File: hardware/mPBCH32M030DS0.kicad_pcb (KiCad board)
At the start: 2 copper layers, 20.3 x 53.3 mm, 90 parts, among them J1 EDGE_L, J2 EDGE_R, J8 USB-C, SW1 RESET, SW2 USER/BOOT, U1 CH32M030C8U7, U3 USBLC6-2SC6, Y1 8MHz CL=20pF

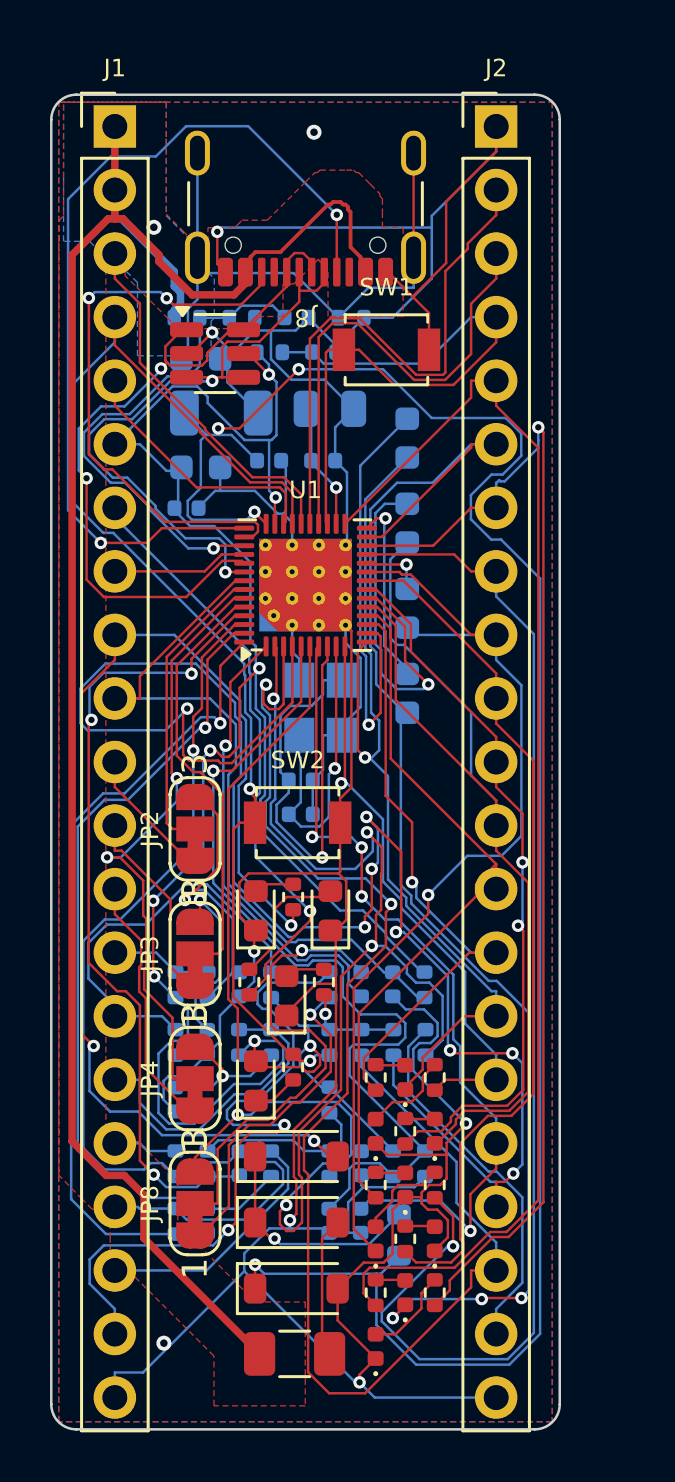
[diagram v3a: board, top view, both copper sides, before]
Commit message: 9マス版に一本化 (8マス版を削除)
- 8 マス版 (20.32mm) は JLCPCB の 2 層標準 0.127mm で配線しきれないため削除
- 9 マス版 (22.86mm, 端子列 0.7in) を hardware/ 直下・hardware/daughter/・hardware/fab/・docs/pcb/ へ移動
- ベタなし版は hardware/nopour/ (図は docs/pcb/nopour/)
- gen_pcb.py から MPB_W9 の切り替えを外し 9 マス固定に。既定ルールは 0.127mm / ビア 0.6/0.3
  (再生成した配置が確定済みの 4 基板と一致することを確認)
- 回路図の注記 (外形・列間) を 22.86mm / 17.78mm に更新し PDF を再出力
- README / stacking.md / design.md を 9 マス版のみの記述に更新

Co-Authored-By: Claude Opus 5.5 <noreply@anthropic.com>
Claude-Session: https://claude.ai/code/session_01LENFjjhDfYjJZV1NWhB9uV
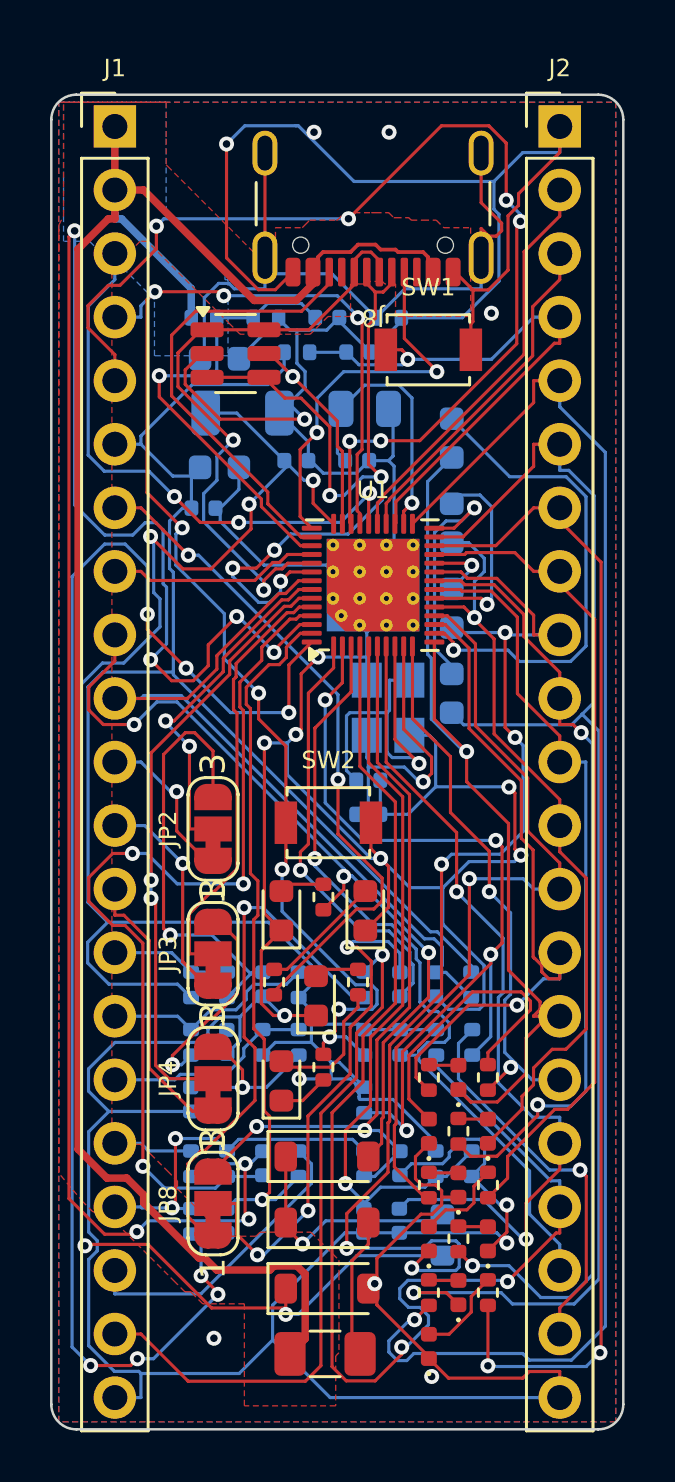
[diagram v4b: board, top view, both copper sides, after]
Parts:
- moved J8 2.70 mm to (12.9, 3.41)
- moved U1 2.70 mm to (12.9, 19.6)
- moved Y1 2.70 mm to (13.5, 24.5)
- moved C131 2.70 mm to (12.7, 27.4)
- moved C132 2.70 mm to (12.7, 28.8)
- moved J2 2.54 mm to (20.3, 1.27)
- moved D10 2.12 mm to (16.3, 39.3)
- moved D11 2.12 mm to (15.1, 41.4)
- moved D12 2.12 mm to (17.4, 41.4)
- moved D13 2.12 mm to (16.3, 43.6)
- moved D14 2.12 mm to (15.1, 45.7)
- moved D15 2.12 mm to (17.4, 45.7)
- moved D16 2.12 mm to (16.3, 47.9)
- moved D17 2.12 mm to (15.1, 50.0)
- moved R50 2.12 mm to (15.1, 39.3)
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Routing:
- net GND: track 197.3 -> 252.5 mm, vias 8 -> 17
- net IA_P: track 31.5 -> 82.6 mm, vias 1 -> 7
- net GPIO_PC5: track 10.5 -> 43.9 mm, vias 0 -> 6
- net IB_N: track 32.5 -> 58.9 mm, vias 1 -> 7
- net I2C_SDA: track 57.7 -> 32.4 mm, vias 2 -> 1
- net USB_CC1: track 36.0 -> 15.4 mm
- net HO2: track 50.2 -> 33.2 mm, vias 1 -> 0
- net VHV: track 80.5 -> 63.7 mm, vias 4 -> 5
- net I2C_SCL: track 70.0 -> 54.5 mm, vias 8 -> 2
- net VBUS: track 46.9 -> 32.8 mm
- net nFAULT: track 44.1 -> 33.7 mm
- net SW1: track 40.5 -> 30.7 mm, vias 0 -> 1
- net SW2: track 38.9 -> 48.5 mm, vias 1 -> 5
- net GPIO_PC4: track 48.8 -> 57.8 mm, vias 2 -> 8
- net GLEDL0: track 3.59 -> 12.2 mm
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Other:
- board size 20.3 x 53.3 mm -> 22.9 x 53.3 mm
